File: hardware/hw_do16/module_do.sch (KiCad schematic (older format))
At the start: 126 parts, among them J1 DO_0, J2 DO_1, J3 MOD, P3 DEBUG, Q1 IRLML5103, Q10 IRLML5103, Q11 IRLML5103, Q12 IRLML5103, Q13 IRLML5103, Q14 IRLML5103, Q15 IRLML5103, Q16 IRLML5103, Q2 IRLML5103, Q3 IRLML5103, Q4 IRLML5103, Q5 IRLML5103, Q6 IRLML5103, Q7 IRLML5103, Q8 IRLML5103, Q9 IRLML5103, U1 STM32F103C8Tx, U2 TLP291-4, U3 TLP291-4, U4 TLP291-4, U5 TLP291-4

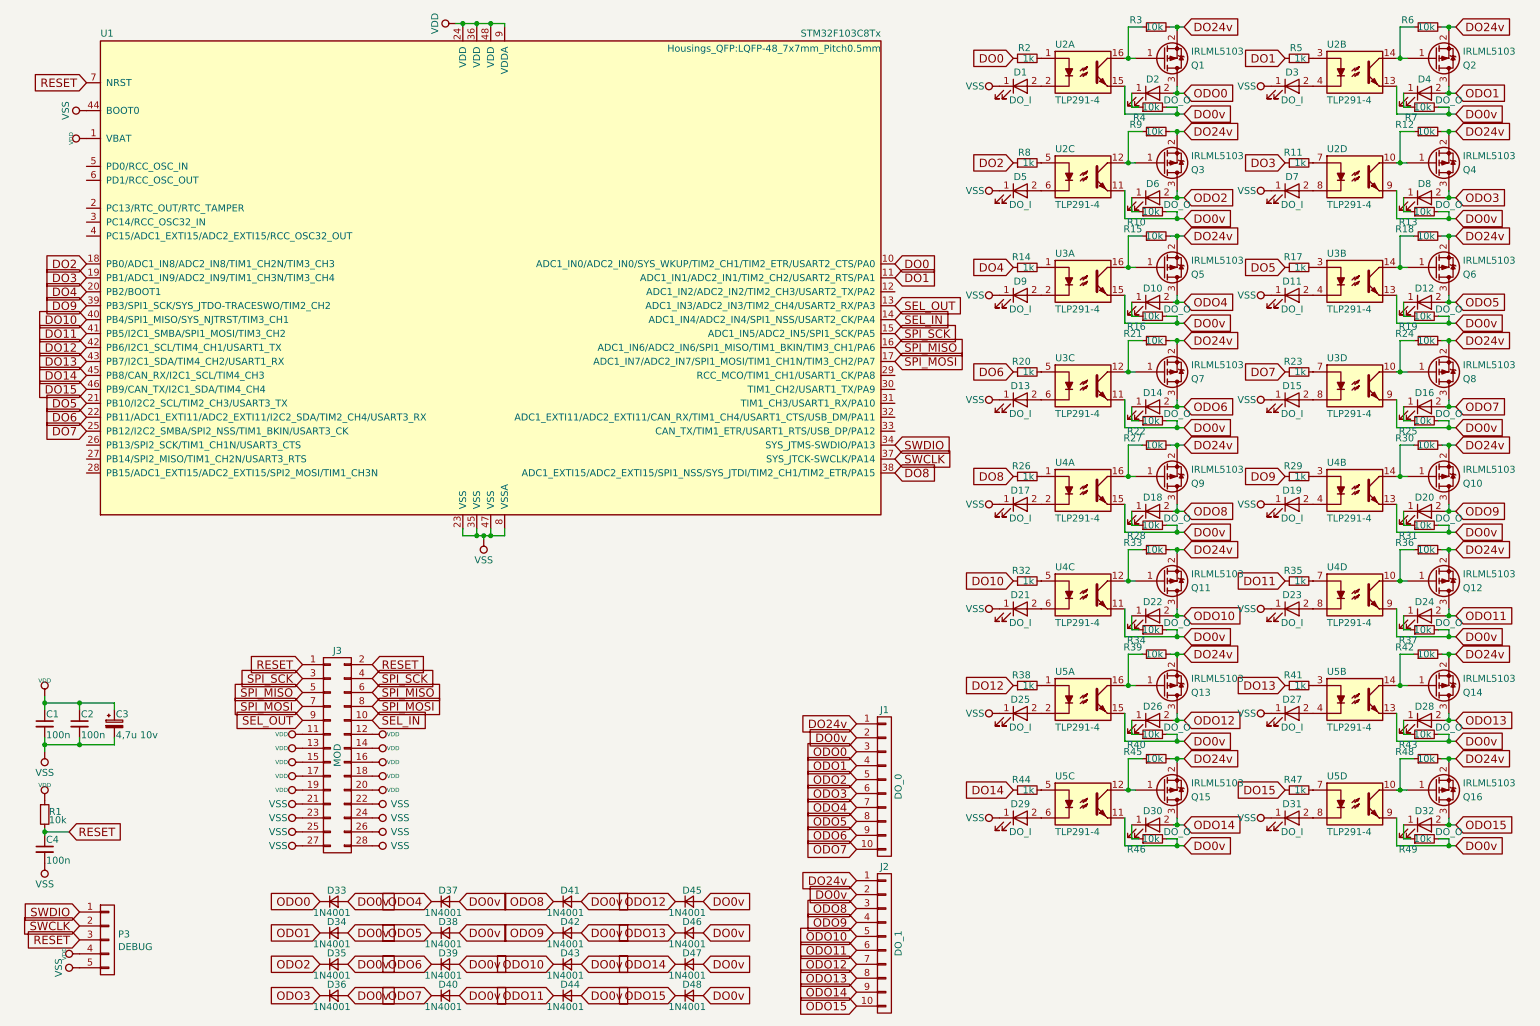
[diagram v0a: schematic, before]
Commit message: Обновлена плата модуля DO16.
Завершена предварительная трассировка.
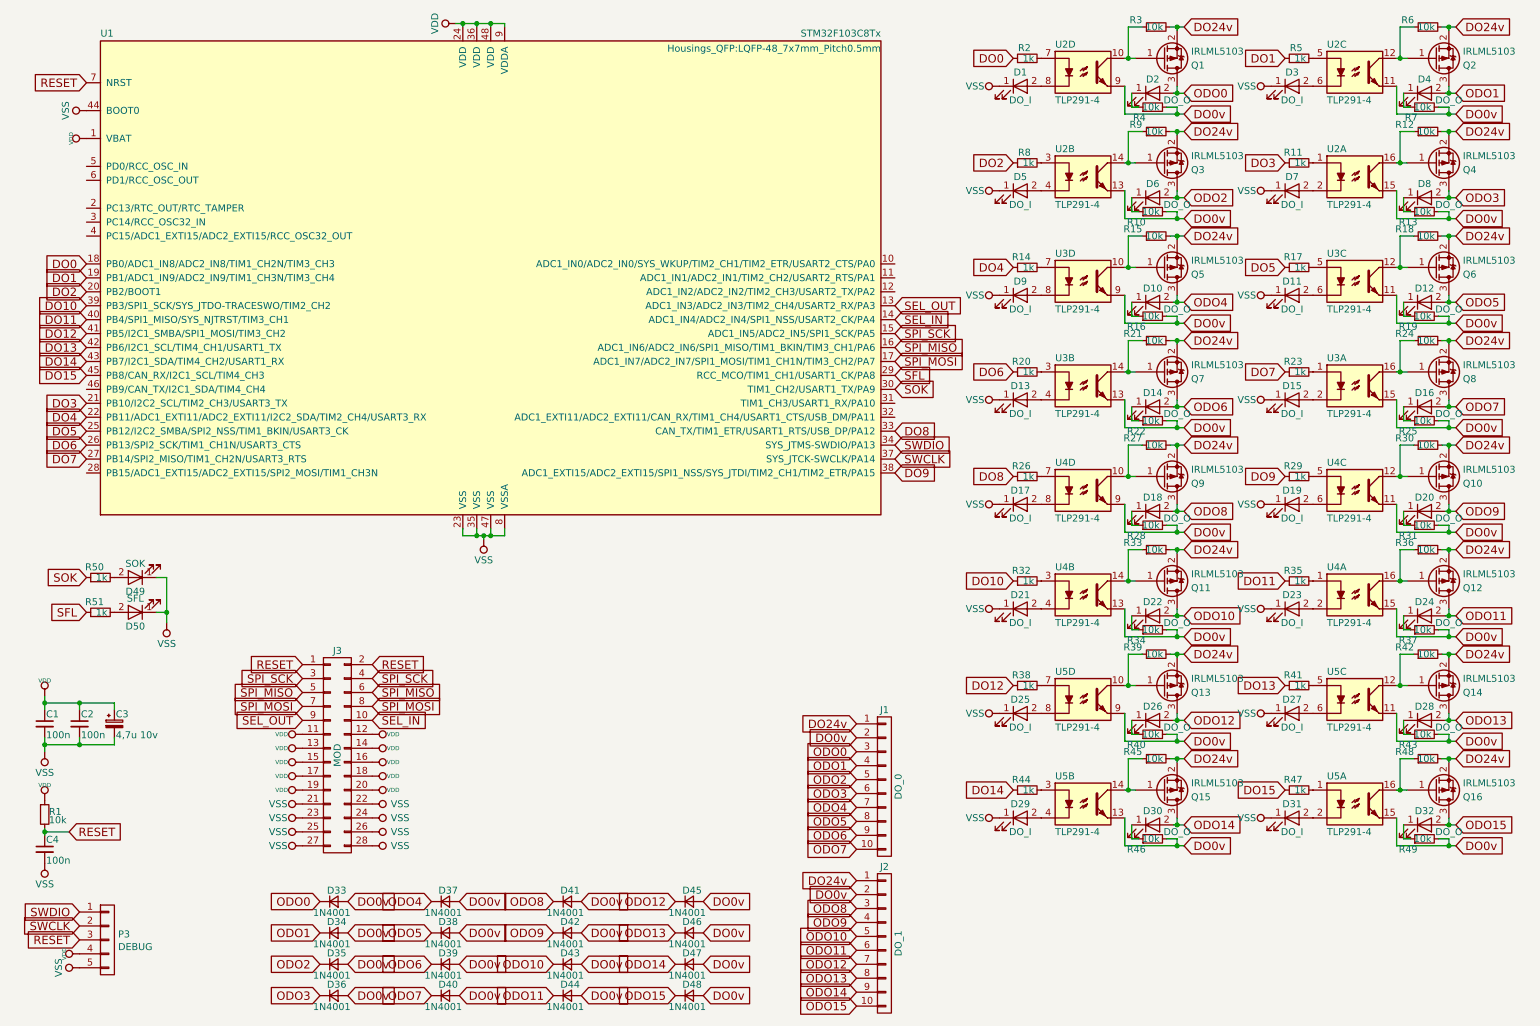
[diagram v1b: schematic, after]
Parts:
- added D49: SOK, LEDs:LED_0603, symbol LED
- added D50: SFL, LEDs:LED_0603, symbol LED
- added R50, R51: 1k, Resistors_SMD:R_0805, symbol R_Small
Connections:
- net DO0: now also U1.18 (PB0/ADC1_IN8/ADC2_IN8/TIM1_CH2N/TIM3_CH3); no longer U1.10 (ADC1_IN0/ADC2_IN0/SYS_WKUP/TIM2_CH1/TIM2_ETR/USART2_CTS/PA0)
- net DO0v: now also U2.11, U2.13, U2.15, U2.9, U3.11, U3.13, U3.15, U3.9, U4.11, U4.13, U4.15, U4.9, U5.11, U5.13, U5.15, U5.9; no longer U2.11, U2.13, U2.15, U2.9, U3.11, U3.13, U3.15, U3.9, U4.11, U4.13, U4.15, U4.9, U5.11, U5.13, U5.15, U5.9
- net DO1: now also U1.19 (PB1/ADC1_IN9/ADC2_IN9/TIM1_CH3N/TIM3_CH4); no longer U1.11 (ADC1_IN1/ADC2_IN1/TIM2_CH2/USART2_RTS/PA1)
- net DO10: now also U1.39 (PB3/SPI1_SCK/SYS_JTDO-TRACESWO/TIM2_CH2); no longer U1.40 (PB4/SPI1_MISO/SYS_NJTRST/TIM3_CH1)
- net DO11: now also U1.40 (PB4/SPI1_MISO/SYS_NJTRST/TIM3_CH1); no longer U1.41 (PB5/I2C1_SMBA/SPI1_MOSI/TIM3_CH2)
- net DO12: now also U1.41 (PB5/I2C1_SMBA/SPI1_MOSI/TIM3_CH2); no longer U1.42 (PB6/I2C1_SCL/TIM4_CH1/USART1_TX)
- net DO13: now also U1.42 (PB6/I2C1_SCL/TIM4_CH1/USART1_TX); no longer U1.43 (PB7/I2C1_SDA/TIM4_CH2/USART1_RX)
- net DO14: now also U1.43 (PB7/I2C1_SDA/TIM4_CH2/USART1_RX); no longer U1.45 (PB8/CAN_RX/I2C1_SCL/TIM4_CH3)
- net DO15: now also U1.45 (PB8/CAN_RX/I2C1_SCL/TIM4_CH3); no longer U1.46 (PB9/CAN_TX/I2C1_SDA/TIM4_CH4)
- net DO2: now also U1.20 (PB2/BOOT1); no longer U1.18 (PB0/ADC1_IN8/ADC2_IN8/TIM1_CH2N/TIM3_CH3)
- net DO3: now also U1.21 (PB10/I2C2_SCL/TIM2_CH3/USART3_TX); no longer U1.19 (PB1/ADC1_IN9/ADC2_IN9/TIM1_CH3N/TIM3_CH4)
- net DO4: now also U1.22 (PB11/ADC1_EXTI11/ADC2_EXTI11/I2C2_SDA/TIM2_CH4/USART3_RX); no longer U1.20 (PB2/BOOT1)
- net DO5: now also U1.25 (PB12/I2C2_SMBA/SPI2_NSS/TIM1_BKIN/USART3_CK); no longer U1.21 (PB10/I2C2_SCL/TIM2_CH3/USART3_TX)
- net DO6: now also U1.26 (PB13/SPI2_SCK/TIM1_CH1N/USART3_CTS); no longer U1.22 (PB11/ADC1_EXTI11/ADC2_EXTI11/I2C2_SDA/TIM2_CH4/USART3_RX)
- net DO7: now also U1.27 (PB14/SPI2_MISO/TIM1_CH2N/USART3_RTS); no longer U1.25 (PB12/I2C2_SMBA/SPI2_NSS/TIM1_BKIN/USART3_CK)
- net DO8: now also U1.33 (CAN_TX/TIM1_ETR/USART1_RTS/USB_DP/PA12); no longer U1.38 (ADC1_EXTI15/ADC2_EXTI15/SPI1_NSS/SYS_JTDI/TIM2_CH1/TIM2_ETR/PA15)
- net DO9: now also U1.38 (ADC1_EXTI15/ADC2_EXTI15/SPI1_NSS/SYS_JTDI/TIM2_CH1/TIM2_ETR/PA15); no longer U1.39 (PB3/SPI1_SCK/SYS_JTDO-TRACESWO/TIM2_CH2)
- net VSS: now also D49.1 (K), D50.1 (K)
- net SFL: now reaches U1.29 (RCC_MCO/TIM1_CH1/USART1_CK/PA8)
- net SFL: now also R51.1
- net SOK: now reaches U1.30 (TIM1_CH2/USART1_TX/PA9)
- net SOK: now also R50.1
- net at R2.2: now also U2.7; no longer U2.1
- net at Q1.1 (G), R3.1: now also U2.10; no longer U2.16
- net at D1.2 (A): now also U2.8; no longer U2.2
- net at Q2.1 (G), R6.1: now also U2.12; no longer U2.14
- net at R5.2: now also U2.5; no longer U2.3
- net at D3.2 (A): now also U2.6; no longer U2.4
- net at Q3.1 (G), R9.1: now also U2.14; no longer U2.12
- net at R8.2: now also U2.3; no longer U2.5
- net at D5.2 (A): now also U2.4; no longer U2.6
- net at Q4.1 (G), R12.1: now also U2.16; no longer U2.10
- net at R11.2: now also U2.1; no longer U2.7
- net at D7.2 (A): now also U2.2; no longer U2.8
- net at R14.2: now also U3.7; no longer U3.1
- net at Q5.1 (G), R15.1: now also U3.10; no longer U3.16
- net at D9.2 (A): now also U3.8; no longer U3.2
- net at Q6.1 (G), R18.1: now also U3.12; no longer U3.14
- net at R17.2: now also U3.5; no longer U3.3
- net at D11.2 (A): now also U3.6; no longer U3.4
- net at Q7.1 (G), R21.1: now also U3.14; no longer U3.12
- net at R20.2: now also U3.3; no longer U3.5
- net at D13.2 (A): now also U3.4; no longer U3.6
- net at Q8.1 (G), R24.1: now also U3.16; no longer U3.10
- net at R23.2: now also U3.1; no longer U3.7
- net at D15.2 (A): now also U3.2; no longer U3.8
- net at R26.2: now also U4.7; no longer U4.1
- net at Q9.1 (G), R27.1: now also U4.10; no longer U4.16
- net at D17.2 (A): now also U4.8; no longer U4.2
- net at Q10.1 (G), R30.1: now also U4.12; no longer U4.14
- net at R29.2: now also U4.5; no longer U4.3
- net at D19.2 (A): now also U4.6; no longer U4.4
- net at Q11.1 (G), R33.1: now also U4.14; no longer U4.12
- net at R32.2: now also U4.3; no longer U4.5
- net at D21.2 (A): now also U4.4; no longer U4.6
- net at Q12.1 (G), R36.1: now also U4.16; no longer U4.10
- net at R35.2: now also U4.1; no longer U4.7
- net at D23.2 (A): now also U4.2; no longer U4.8
- net at R38.2: now also U5.7; no longer U5.1
- net at Q13.1 (G), R39.1: now also U5.10; no longer U5.16
- net at D25.2 (A): now also U5.8; no longer U5.2
- net at Q14.1 (G), R42.1: now also U5.12; no longer U5.14
- net at R41.2: now also U5.5; no longer U5.3
- net at D27.2 (A): now also U5.6; no longer U5.4
- net at Q15.1 (G), R45.1: now also U5.14; no longer U5.12
- net at R44.2: now also U5.3; no longer U5.5
- net at D29.2 (A): now also U5.4; no longer U5.6
- net at Q16.1 (G), R48.1: now also U5.16; no longer U5.10
- net at R47.2: now also U5.1; no longer U5.7
- net at D31.2 (A): now also U5.2; no longer U5.8
- new net: D49.2 (A), R50.2
- new net: D50.2 (A), R51.2
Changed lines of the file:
@@
 Comment4 ""
 $EndDescr
-Text GLabel 6725 2300 2    60   Input ~ 0
+Text GLabel 925  2300 0    60   Input ~ 0
 DO0
-Text GLabel 6725 2400 2    60   Input ~ 0
+Text GLabel 925  2400 0    60   Input ~ 0
 DO1
-Text GLabel 925  2300 0    60   Input ~ 0
+Text GLabel 925  2500 0    60   Input ~ 0
 DO2
-Text GLabel 925  2400 0    60   Input ~ 0
+Text GLabel 925  3300 0    60   Input ~ 0
 DO3
-Text GLabel 925  2500 0    60   Input ~ 0
+Text GLabel 925  3400 0    60   Input ~ 0
 DO4
-Text GLabel 925  3300 0    60   Input ~ 0
+Text GLabel 925  3500 0    60   Input ~ 0
 DO5
-Text GLabel 925  3400 0    60   Input ~ 0
+Text GLabel 925  3600 0    60   Input ~ 0
 DO6
-Text GLabel 925  3500 0    60   Input ~ 0
+Text GLabel 925  3700 0    60   Input ~ 0
 DO7
+Text GLabel 6725 3500 2    60   Input ~ 0
+DO8
 Text GLabel 6725 3800 2    60   Input ~ 0
-DO8
+DO9
 Text GLabel 925  2600 0    60   Input ~ 0
-DO9
+DO10
 Text GLabel 925  2700 0    60   Input ~ 0
-DO10
+DO11
 Text GLabel 925  2800 0    60   Input ~ 0
-DO11
+DO12
 Text GLabel 925  2900 0    60   Input ~ 0
-DO12
+DO13
 Text GLabel 925  3000 0    60   Input ~ 0
-DO13
+DO14
 Text GLabel 925  3100 0    60   Input ~ 0
-DO14
-Text GLabel 925  3200 0    60   Input ~ 0
 DO15
 Text GLabel 6450 5800 0    60   Input ~ 0
@@
 $Comp
 L TLP291-4 U2
-U 1 1 5949324F
+U 4 1 5949324F
 P 8075 925
 F 0 "U2" H 7875 1125 50  0000 L CNN
@@
 F 2 "SMD_Packages:SO-16-N" H 7875 725 50  0001 L CIN
 F 3 "" H 8075 925 50  0000 L CNN
-	1    8075 925
+	4    8075 925
 	1    0    0    -1
 $EndComp
@@
 $Comp
 L TLP291-4 U2
-U 2 1 5996284D
+U 3 1 5996284D
 P 10025 925
 F 0 "U2" H 9825 1125 50  0000 L CNN
@@
 F 2 "SMD_Packages:SO-16-N" H 9825 725 50  0001 L CIN
 F 3 "" H 10025 925 50  0000 L CNN
-	2    10025 925
+	3    10025 925
 	1    0    0    -1
 $EndComp
@@
 $Comp
 L TLP291-4 U2
-U 3 1 59962D26
+U 2 1 59962D26
 P 8075 1675
 F 0 "U2" H 7875 1875 50  0000 L CNN
@@
 F 2 "SMD_Packages:SO-16-N" H 7875 1475 50  0001 L CIN
 F 3 "" H 8075 1675 50  0000 L CNN
-	3    8075 1675
+	2    8075 1675
 	1    0    0    -1
 $EndComp
@@
 $Comp
 L TLP291-4 U2
-U 4 1 59962D6F
+U 1 1 59962D6F
 P 10025 1675
 F 0 "U2" H 9825 1875 50  0000 L CNN
@@
 F 2 "SMD_Packages:SO-16-N" H 9825 1475 50  0001 L CIN
 F 3 "" H 10025 1675 50  0000 L CNN
-	4    10025 1675
+	1    10025 1675
 	1    0    0    -1
 $EndComp
@@
 $Comp
 L TLP291-4 U3
-U 1 1 59963D00
+U 4 1 59963D00
 P 8075 2425
 F 0 "U3" H 7875 2625 50  0000 L CNN
@@
 F 2 "SMD_Packages:SO-16-N" H 7875 2225 50  0001 L CIN
 F 3 "" H 8075 2425 50  0000 L CNN
-	1    8075 2425
+	4    8075 2425
 	1    0    0    -1
 $EndComp
@@
 $Comp
 L TLP291-4 U3
-U 2 1 59963D49
+U 3 1 59963D49
 P 10025 2425
 F 0 "U3" H 9825 2625 50  0000 L CNN
@@
 F 2 "SMD_Packages:SO-16-N" H 9825 2225 50  0001 L CIN
 F 3 "" H 10025 2425 50  0000 L CNN
-	2    10025 2425
+	3    10025 2425
 	1    0    0    -1
 $EndComp
@@
 $Comp
 L TLP291-4 U3
-U 3 1 59963D92
+U 2 1 59963D92
 P 8075 3175
 F 0 "U3" H 7875 3375 50  0000 L CNN
@@
 F 2 "SMD_Packages:SO-16-N" H 7875 2975 50  0001 L CIN
 F 3 "" H 8075 3175 50  0000 L CNN
-	3    8075 3175
+	2    8075 3175
 	1    0    0    -1
 $EndComp
@@
 $Comp
 L TLP291-4 U3
-U 4 1 59963DDB
+U 1 1 59963DDB
 P 10025 3175
 F 0 "U3" H 9825 3375 50  0000 L CNN
@@
 F 2 "SMD_Packages:SO-16-N" H 9825 2975 50  0001 L CIN
 F 3 "" H 10025 3175 50  0000 L CNN
-	4    10025 3175
+	1    10025 3175
 	1    0    0    -1
 $EndComp
@@
 $Comp
 L TLP291-4 U4
-U 1 1 5996654C
+U 4 1 5996654C
 P 8075 3925
 F 0 "U4" H 7875 4125 50  0000 L CNN
@@
 F 2 "SMD_Packages:SO-16-N" H 7875 3725 50  0001 L CIN
 F 3 "" H 8075 3925 50  0000 L CNN
-	1    8075 3925
+	4    8075 3925
 	1    0    0    -1
 $EndComp
@@
 $Comp
 L TLP291-4 U4
-U 2 1 59966595
+U 3 1 59966595
 P 10025 3925
 F 0 "U4" H 9825 4125 50  0000 L CNN
@@
 F 2 "SMD_Packages:SO-16-N" H 9825 3725 50  0001 L CIN
 F 3 "" H 10025 3925 50  0000 L CNN
-	2    10025 3925
+	3    10025 3925
 	1    0    0    -1
 $EndComp
@@
 $Comp
 L TLP291-4 U4
-U 3 1 599665DE
+U 2 1 599665DE
 P 8075 4675
 F 0 "U4" H 7875 4875 50  0000 L CNN
@@
 F 2 "SMD_Packages:SO-16-N" H 7875 4475 50  0001 L CIN
 F 3 "" H 8075 4675 50  0000 L CNN
-	3    8075 4675
+	2    8075 4675
 	1    0    0    -1
 $EndComp
@@
 $Comp
 L TLP291-4 U4
-U 4 1 59966627
+U 1 1 59966627
 P 10025 4675
 F 0 "U4" H 9825 4875 50  0000 L CNN
@@
 F 2 "SMD_Packages:SO-16-N" H 9825 4475 50  0001 L CIN
 F 3 "" H 10025 4675 50  0000 L CNN
-	4    10025 4675
+	1    10025 4675
 	1    0    0    -1
 $EndComp
@@
 $Comp
 L TLP291-4 U5
-U 1 1 59966670
+U 4 1 59966670
 P 8075 5425
 F 0 "U5" H 7875 5625 50  0000 L CNN
@@
 F 2 "SMD_Packages:SO-16-N" H 7875 5225 50  0001 L CIN
 F 3 "" H 8075 5425 50  0000 L CNN
-	1    8075 5425
+	4    8075 5425
 	1    0    0    -1
 $EndComp
@@
 $Comp
 L TLP291-4 U5
-U 2 1 599666B9
+U 3 1 599666B9
 P 10025 5425
 F 0 "U5" H 9825 5625 50  0000 L CNN
@@
 F 2 "SMD_Packages:SO-16-N" H 9825 5225 50  0001 L CIN
 F 3 "" H 10025 5425 50  0000 L CNN
-	2    10025 5425
+	3    10025 5425
 	1    0    0    -1
 $EndComp
@@
 $Comp
 L TLP291-4 U5
-U 3 1 59966702
+U 2 1 59966702
 P 8075 6175
 F 0 "U5" H 7875 6375 50  0000 L CNN
@@
 F 2 "SMD_Packages:SO-16-N" H 7875 5975 50  0001 L CIN
 F 3 "" H 8075 6175 50  0000 L CNN
-	3    8075 6175
+	2    8075 6175
 	1    0    0    -1
 $EndComp
@@
 $Comp
 L TLP291-4 U5
-U 4 1 5996674B
+U 1 1 5996674B
 P 10025 6175
 F 0 "U5" H 9825 6375 50  0000 L CNN
@@
 F 2 "SMD_Packages:SO-16-N" H 9825 5975 50  0001 L CIN
 F 3 "" H 10025 6175 50  0000 L CNN
-	4    10025 6175
+	1    10025 6175
 	1    0    0    -1
 $EndComp
@@
 	0    -1   -1   0
 $EndComp
+$Comp
+L LED D49
+U 1 1 5996B9A4
+P 1275 4550
+F 0 "D49" H 1275 4650 50  0000 C CNN
+F 1 "SOK" H 1275 4450 50  0000 C CNN
+F 2 "LEDs:LED_0603" H 1275 4550 50  0001 C CNN
+F 3 "" H 1275 4550 50  0001 C CNN
+	1    1275 4550
+	-1   0    0    1
+$EndComp
+$Comp
+L LED D50
+U 1 1 5996BE28
+P 1275 4800
+F 0 "D50" H 1275 4900 50  0000 C CNN
+F 1 "SFL" H 1275 4700 50  0000 C CNN
+F 2 "LEDs:LED_0603" H 1275 4800 50  0001 C CNN
+F 3 "" H 1275 4800 50  0001 C CNN
+	1    1275 4800
+	-1   0    0    1
+$EndComp
+Text GLabel 925  4550 0    60   Input ~ 0
+SOK
+Text GLabel 925  4800 0    60   Input ~ 0
+SFL
+$Comp
+L R_Small R50
+U 1 1 5996D95B
+P 1025 4550
+F 0 "R50" V 1100 4525 50  0000 L CNN
+F 1 "1k" V 1025 4500 50  0000 L CNN
+F 2 "Resistors_SMD:R_0805" H 1025 4550 50  0001 C CNN
+F 3 "" H 1025 4550 50  0000 C CNN
+	1    1025 4550
+	0    -1   -1   0
+$EndComp
+$Comp
+L R_Small R51
+U 1 1 5996DD59
+P 1025 4800
+F 0 "R51" V 1100 4775 50  0000 L CNN
+F 1 "1k" V 1025 4750 50  0000 L CNN
+F 2 "Resistors_SMD:R_0805" H 1025 4800 50  0001 C CNN
+F 3 "" H 1025 4800 50  0000 C CNN
+	1    1025 4800
+	0    -1   -1   0
+$EndComp
+$Comp
+L VSS #PWR045
+U 1 1 5996F50B
+P 1500 4875
+F 0 "#PWR045" H 1500 4725 50  0001 C CNN
+F 1 "VSS" H 1500 5025 50  0000 C CNN
+F 2 "" H 1500 4875 50  0000 C CNN
+F 3 "" H 1500 4875 50  0000 C CNN
+	1    1500 4875
+	-1   0    0    1
+$EndComp
+Wire Wire Line
+	1425 4550 1500 4550
+Wire Wire Line
+	1500 4550 1500 4875
+Wire Wire Line
+	1425 4800 1500 4800
+Connection ~ 1500 4800
+Text GLabel 6725 3200 2    60   Input ~ 0
+SOK
+Text GLabel 6725 3100 2    60   Input ~ 0
+SFL
 $EndSCHEMATC
